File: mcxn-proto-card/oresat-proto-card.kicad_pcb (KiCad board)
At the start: 4 copper layers, 99.8 x 94.6 mm, 141 parts, among them J1 J-SAMTEC-TFM-120-X1-XXX-D-RA, J10 61083-061409LF, J11 436500201, J14 ESQ-126-12-G-D, J15 ESQ-126-12-G-D, J3 SM14B-SHLS-TF, Q1 DMP2240UDM, Q2 DMP3050LVT-7, Q7 DMP3050LVT-7, Q8 PMV45EN, Q9 PMV45EN, U1 MCXN947VKLT, U10 TPS62111RSA, U11 MIC842LYC5, U12 MIC842LYC5, U2 MAX7310, U3 TS5A21366DCUR, U6 MAX4211FETE, U8 TCAN330, Y2 24 MHz

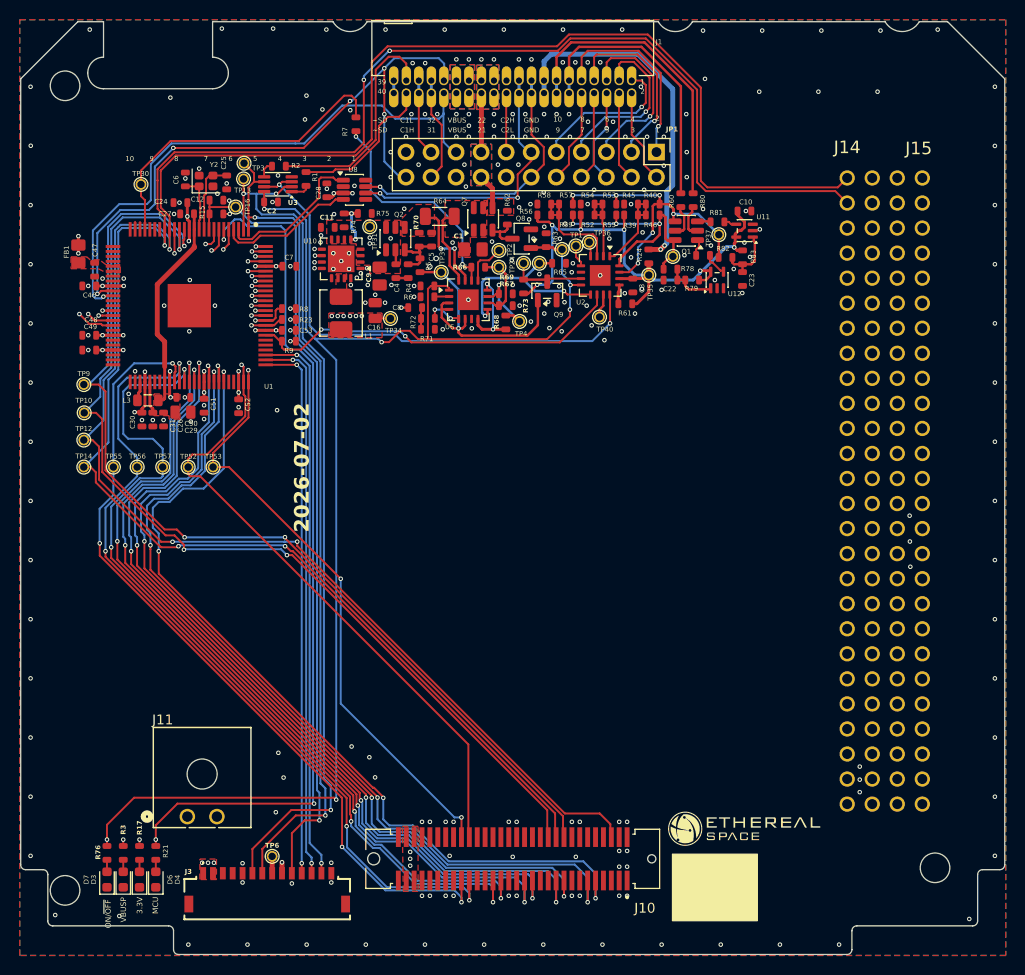
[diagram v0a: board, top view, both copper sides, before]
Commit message: Finalized design with adding properly measured mounting holes that line up with piPlasma.
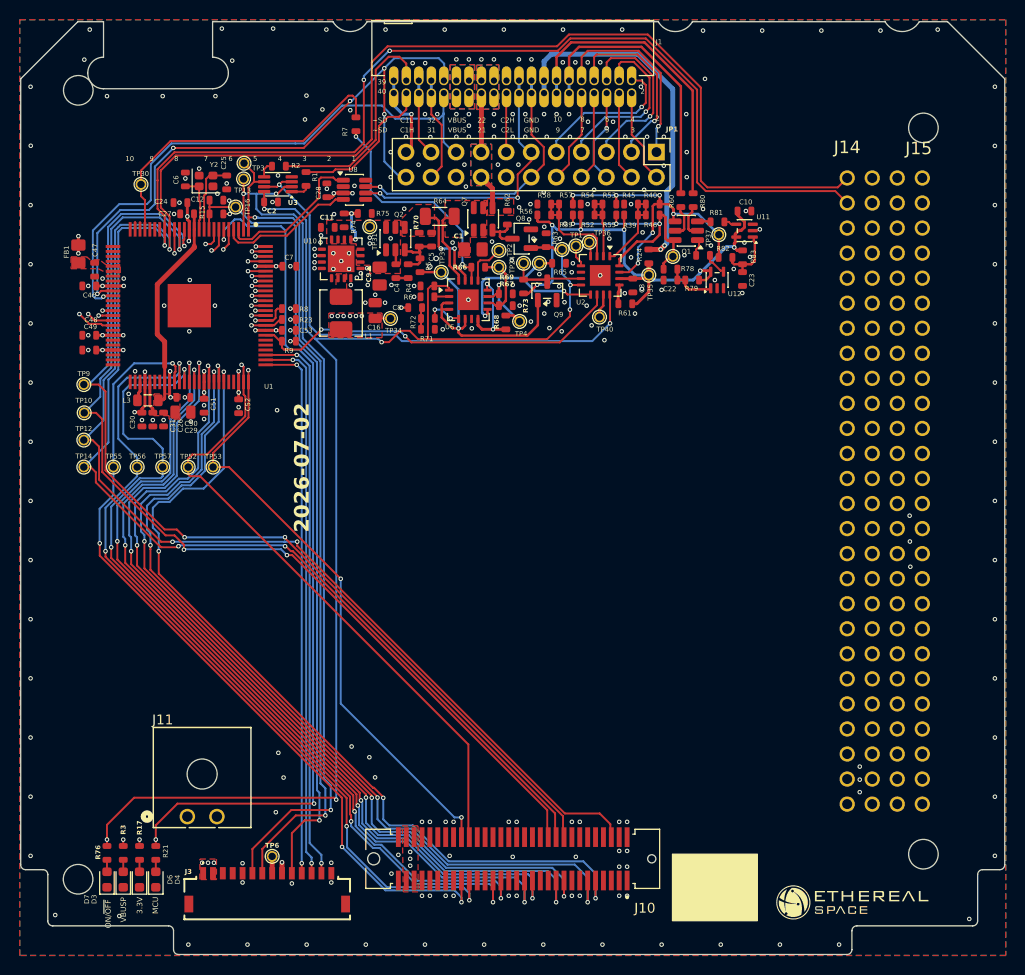
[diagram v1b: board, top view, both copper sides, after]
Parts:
- moved G*** 13.3 mm to (183.1, 146.8)
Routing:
- net /~{SD}: track 1.51 -> 8.99 mm, vias 0 -> 1
- net GND: vias 260 -> 263

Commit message: Finalized design with adding properly measured mounting holes that line up with piPlasma. As well as changing sense resistor to allow 1A trip
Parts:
- R64: value 100m -> 30m
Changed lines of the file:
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@@
 			)
 		)
-		(property "Value" "100m"
+		(property "Value" "30m"
 			(at 0 1.83 180)
 			(layer "F.Fab")
@@
 			)
 		)
-		(property "Description" "100 mOhms ±1% 0.5W, 1/2W Chip Resistor 1206 (3216 Metric) Current Sense Thick Film"
+		(property "Description" "RES 0.03 OHM 1% 1/2W 1206"
 			(at 0 0 180)
 			(layer "F.Fab")
@@
 			)
 		)
-		(property "DPN" "CSR1206FKR100CT-ND"
+		(property "DPN" "CSR1206FK30L0TR-ND"
 			(at 0 0 180)
 			(unlocked yes)
@@
 			)
 		)
-		(property "MPN" "CSR1206FKR100"
+		(property "MPN" "CSR1206FK30L0"
 			(at 0 0 180)
 			(unlocked yes)
@@
 		(sheetname "/")
 		(sheetfile "oresat-proto-card.kicad_sch")
+		(units
+			(unit
+				(name "A")
+				(pins)
+			)
+		)
 		(duplicate_pad_numbers_are_jumpers no)
 		(fp_poly
@@
 		)
 		(min_thickness 0.127)
-		(fill yes
+		(fill
 			(thermal_gap 0.127)
 			(thermal_bridge_width 0.5)
@@
 		)
 		(min_thickness 0.127)
-		(fill yes
+		(fill
 			(thermal_gap 0.5)
 			(thermal_bridge_width 0.5)
@@
 		)
 		(min_thickness 0.15)
-		(fill yes
+		(fill
 			(thermal_gap 0.5)
 			(thermal_bridge_width 0.5)
@@
 		)
 		(min_thickness 0.0635)
-		(fill yes
+		(fill
 			(thermal_gap 0.5)
 			(thermal_bridge_width 0.5)
@@
 		)
 		(min_thickness 0.127)
-		(fill yes
+		(fill
 			(thermal_gap 0.5)
 			(thermal_bridge_width 0.5)
@@
 		)
 		(min_thickness 0.127)
-		(fill yes
+		(fill
 			(thermal_gap 0.5)
 			(thermal_bridge_width 0.5)
@@
 		)
 		(min_thickness 0.0635)
-		(fill yes
+		(fill
 			(thermal_gap 0.5)
 			(thermal_bridge_width 0.5)
@@
 		)
 		(min_thickness 0.127)
-		(fill yes
+		(fill
 			(thermal_gap 0.5)
 			(thermal_bridge_width 0.5)
@@
 		)
 		(min_thickness 0.0635)
-		(fill yes
+		(fill
 			(thermal_gap 0.5)
 			(thermal_bridge_width 0.5)
@@
 		)
 		(min_thickness 0.127)
-		(fill yes
+		(fill
 			(thermal_gap 0.5)
 			(thermal_bridge_width 0.5)
@@
 		)
 		(min_thickness 0.127)
-		(fill yes
+		(fill
 			(thermal_gap 0.5)
 			(thermal_bridge_width 0.5)
@@
 		)
 		(min_thickness 0.0635)
-		(fill yes
+		(fill
 			(thermal_gap 0.5)
 			(thermal_bridge_width 0.5)
@@
 		)
 		(min_thickness 0.0635)
-		(fill yes
+		(fill
 			(thermal_gap 0.5)
 			(thermal_bridge_width 0.5)
@@
 		)
 		(min_thickness 0.127)
-		(fill yes
+		(fill
 			(thermal_gap 0.127)
 			(thermal_bridge_width 0.5)
@@
 		)
 		(min_thickness 0.0762)
-		(fill yes
+		(fill
 			(thermal_gap 0.5)
 			(thermal_bridge_width 0.5)
@@
 		)
 		(min_thickness 0.127)
-		(fill yes
+		(fill
 			(thermal_gap 0)
 			(thermal_bridge_width 0.5)
@@
 		)
 		(min_thickness 0.127)
-		(fill yes
+		(fill
 			(thermal_gap 0.127)
 			(thermal_bridge_width 0.5)
@@
 		)
 		(min_thickness 0.0635)
-		(fill yes
+		(fill
 			(thermal_gap 0.177)
 			(thermal_bridge_width 0.177)
